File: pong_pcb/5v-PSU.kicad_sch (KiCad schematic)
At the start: 15 parts, among them U2 LMR23630APQDRRTQ1

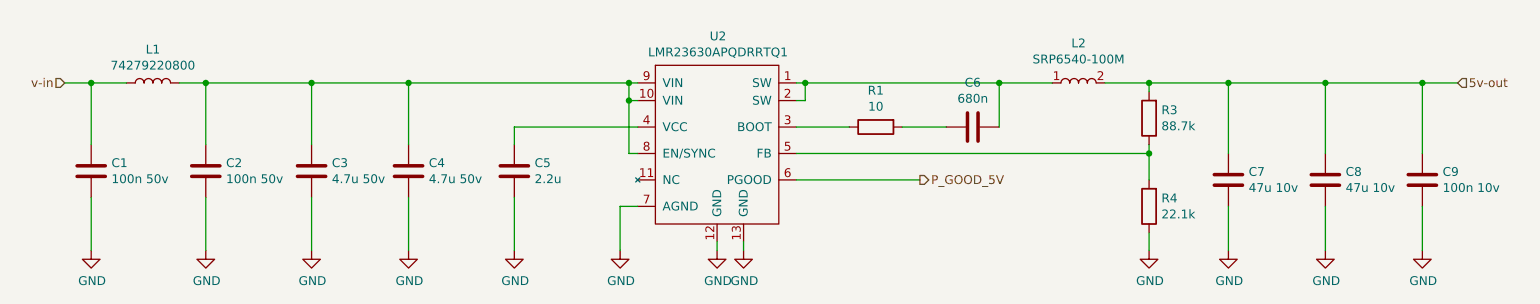
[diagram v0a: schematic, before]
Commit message: Update schema and add packages
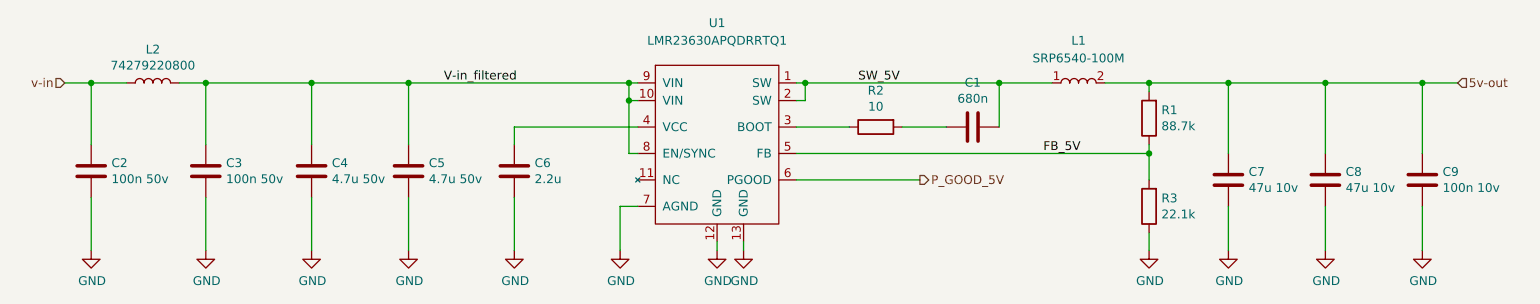
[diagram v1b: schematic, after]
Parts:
- removed L2: SRP6540-100M, 3ABuck:SRP6540-100M, symbol 3Abuck:SRP6540-100M
- removed U2: LMR23630APQDRRTQ1, 3ABuck:LMR23630APQDRRTQ1, symbol 3Abuck:LMR23630APQDRRTQ1
- added L1: SRP6540-100M, MyLib:SRP6540-100M, symbol MyLib:SRP6540-100M
- added U1: LMR23630APQDRRTQ1, MyLib:LMR23630APQDRRTQ1, symbol MyLib:LMR23630APQDRRTQ1
- C7, C8: footprint Capacitor_SMD:C_1206_3216Metric_Pad1.42x1.75mm_HandSolder -> Capacitor_SMD:C_1206_3216Metric_Pad1.33x1.80mm_HandSolder
- R1: renamed from R3; footprint Resistor_SMD:R_0402_1005Metric_Pad0.72x0.64mm_HandSolder -> Resistor_SMD:R_0603_1608Metric
- R2: renamed from R1; footprint Resistor_SMD:R_0402_1005Metric_Pad0.72x0.64mm_HandSolder -> Resistor_SMD:R_0603_1608Metric
- R3: renamed from R4; footprint Resistor_SMD:R_0402_1005Metric_Pad0.72x0.64mm_HandSolder -> Resistor_SMD:R_0603_1608Metric
- renumbered C6 to C1, C1 to C2, C2 to C3, C3 to C4, C4 to C5, C5 to C6, L1 to L2
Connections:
- net 5v-out: now also L1.2
- net GND: now also U1.12 (GND), U1.13 (GND), U1.7 (AGND)
- net P_GOOD_5V: now also U1.6 (PGOOD)
- net V-in_filtered: now reaches C3.1, C4.1, C5.1, L2.2
- net V-in_filtered: now also U1.10 (VIN), U1.8 (EN/SYNC), U1.9 (VIN)
- net at R2.1: now also U1.3 (BOOT)
- net SW_5V: now reaches C1.1
- net SW_5V: now also L1.1, U1.1 (SW), U1.2 (SW)
- net at C6.1: now also U1.4 (VCC)
- net FB_5V: now reaches R1.1, R3.2
- net FB_5V: now also U1.5 (FB)
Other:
- company: (none) -> Fontys
- title: (none) -> 5V power supply

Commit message: Add HDMI layout
And others
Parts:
- C6: footprint Capacitor_SMD:C_0402_1005Metric_Pad0.74x0.62mm_HandSolder -> Capacitor_SMD:C_0603_1608Metric_Pad1.08x0.95mm_HandSolder
- C9: footprint Capacitor_SMD:C_0402_1005Metric_Pad0.74x0.62mm_HandSolder -> Capacitor_SMD:C_0603_1608Metric
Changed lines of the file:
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@@
 			)
 		)
-		(property "Footprint" "Capacitor_SMD:C_0402_1005Metric_Pad0.74x0.62mm_HandSolder"
+		(property "Footprint" "Capacitor_SMD:C_0603_1608Metric"
 			(at 240.9952 101.6 0)
 			(effects
@@
 			)
 		)
-		(property "Footprint" "Capacitor_SMD:C_0402_1005Metric_Pad0.74x0.62mm_HandSolder"
+		(property "Footprint" "Capacitor_SMD:C_0603_1608Metric_Pad1.08x0.95mm_HandSolder"
 			(at 110.1852 100.33 0)
 			(effects
